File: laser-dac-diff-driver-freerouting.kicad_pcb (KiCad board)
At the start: 2 copper layers, 70.5 x 51.4 mm, 55 parts, among them IC401 DCDC-CONV_TRACO_TMH-XXXX_Dual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, P101 CONN_2, P102 CONN_3X2, P103 CONN_6X2, U101 AD5689RARUZ, U102 74HC04, U201 OP470, U202 LM358, U401 LM317EMP, U402 LM317EMP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

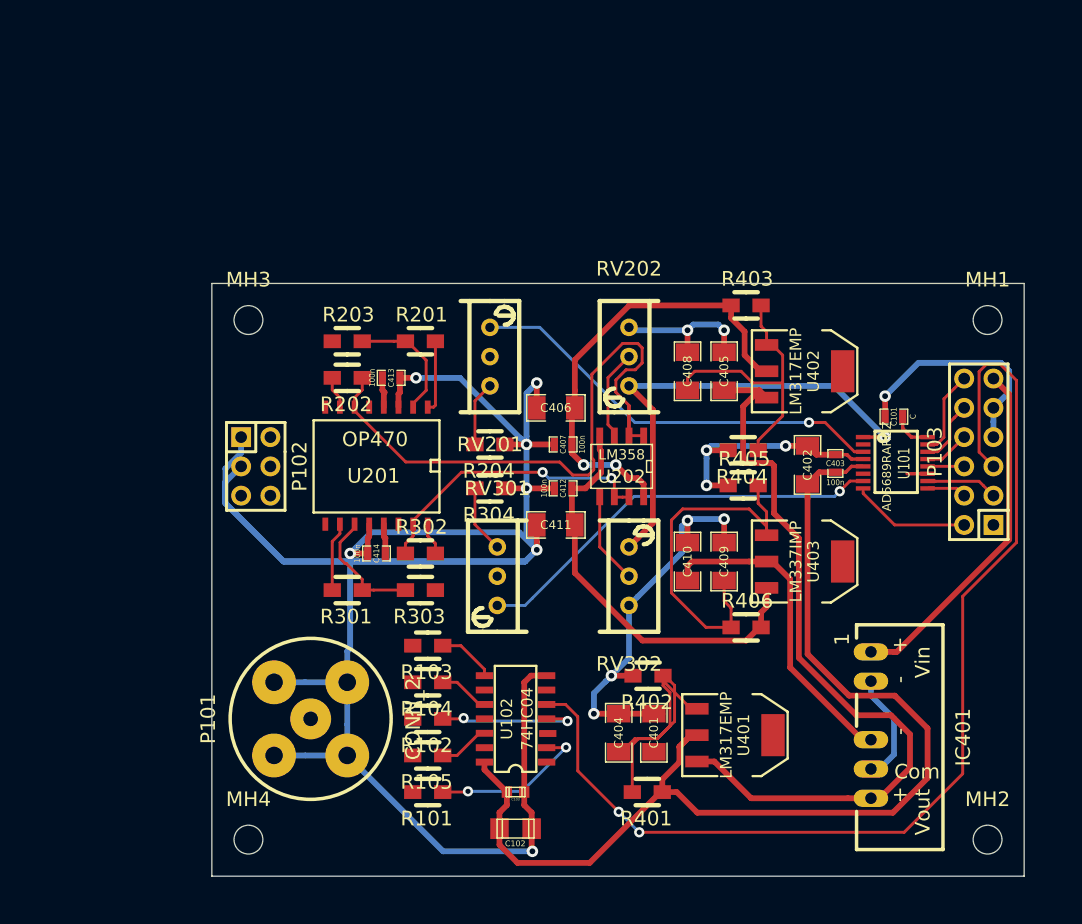
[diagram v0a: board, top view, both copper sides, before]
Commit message: A few autorouter attempts and a new board layout (component positions). Removed voltage selector for MOD driver, 5V only now.
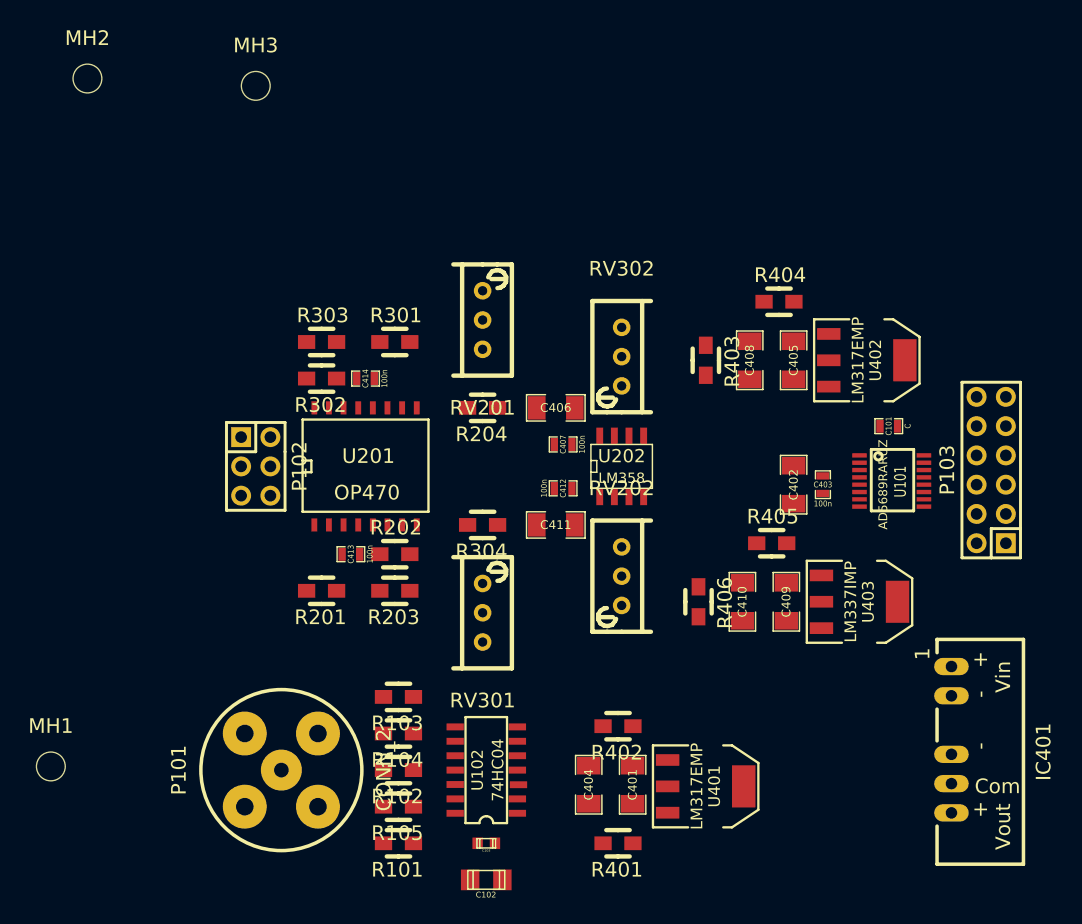
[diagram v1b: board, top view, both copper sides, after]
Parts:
- removed the MH3 at (201.9, 37.5)
- moved MH2 102.3 mm to (188.0, 16.5)
- moved MH3 66.7 mm to (202.6, 17.1)
- moved R201 23.3 mm to (208.3, 61.0), turned to 180 degrees
- moved R303 23.2 mm to (208.3, 39.4), turned to 0 degrees
- moved R203 22.0 mm to (214.6, 61.0), turned to 180 degrees
- moved R301 21.9 mm to (214.6, 39.4), turned to 0 degrees
- moved RV202 19.1 mm to (234.3, 59.7)
- moved RV302 19.1 mm to (234.3, 40.6), turned to 0 degrees
- moved MH1 18.3 mm to (184.8, 76.2)
- moved R302 17.4 mm to (208.3, 42.5), turned to 180 degrees
- moved R202 15.9 mm to (214.6, 57.8), turned to 0 degrees
- moved C413 15.7 mm to (210.8, 57.8), turned to 180 degrees
- moved C414 15.2 mm to (212.1, 42.5), turned to 180 degrees
- moved R404 13.3 mm to (248.0, 35.9), turned to 0 degrees
- moved IC401 7.10 mm to (265.4, 74.9)
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- renumbered MH4 to MH1, MH1 to MH3
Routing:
- net DGND: track 300.9 -> 0.00 mm, vias 17 -> 0
- net +5VD: track 96.1 -> 0.00 mm
- net /MOD_IN: track 94.4 -> 0.00 mm, vias 2 -> 0
- net /powersupply/+Vout_unreg: track 67.3 -> 0.00 mm
- net Net-(R202-Pad1): track 53.8 -> 0.00 mm
- net VAA: track 42.1 -> 0.00 mm, vias 2 -> 0
- net /analog/+Vref: track 41.7 -> 0.00 mm, vias 1 -> 0
- net -VAA: track 39.1 -> 0.00 mm
- net /analog/In1: track 36.9 -> 0.00 mm, vias 1 -> 0
- net /analog2/In1: track 36.2 -> 0.00 mm, vias 1 -> 0
- net Net-(C409-Pad2): track 31.7 -> 0.00 mm
- net /powersupply/+Vin: track 30.6 -> 0.00 mm
- net /powersupply/-Vout_unreg: track 28.7 -> 0.00 mm
- net Net-(C404-Pad1): track 27.5 -> 0.00 mm
- net Net-(R302-Pad1): track 25.3 -> 0.00 mm, vias 2 -> 0
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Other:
- board outline removed
